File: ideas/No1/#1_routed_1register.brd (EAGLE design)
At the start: 85.1 x 137.5 mm, 20 parts, among them P1-O8RIGHT TD620831A, P1-P8LEFT TD620831A, U1 SN74HC595N, U2 SN74HC595N, U3 SN74HC595N

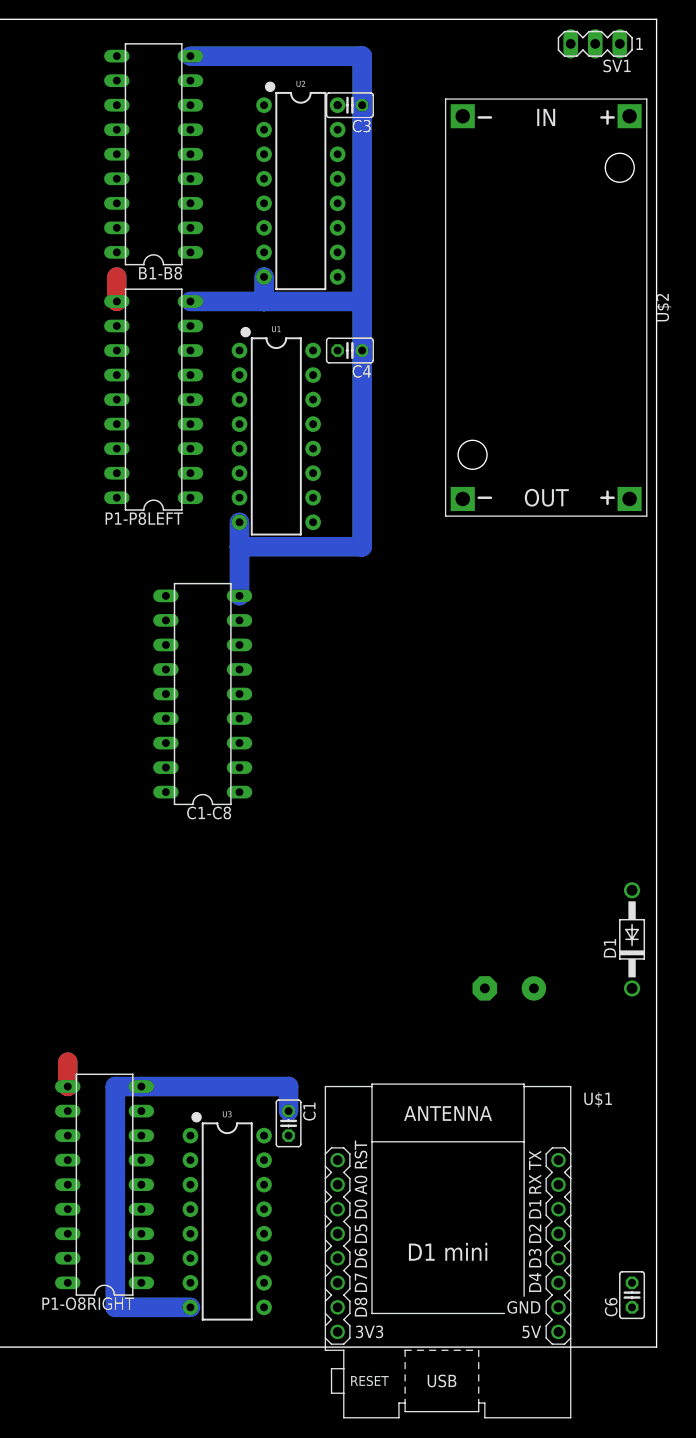
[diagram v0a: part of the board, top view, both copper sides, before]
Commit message: update picture with cable pins
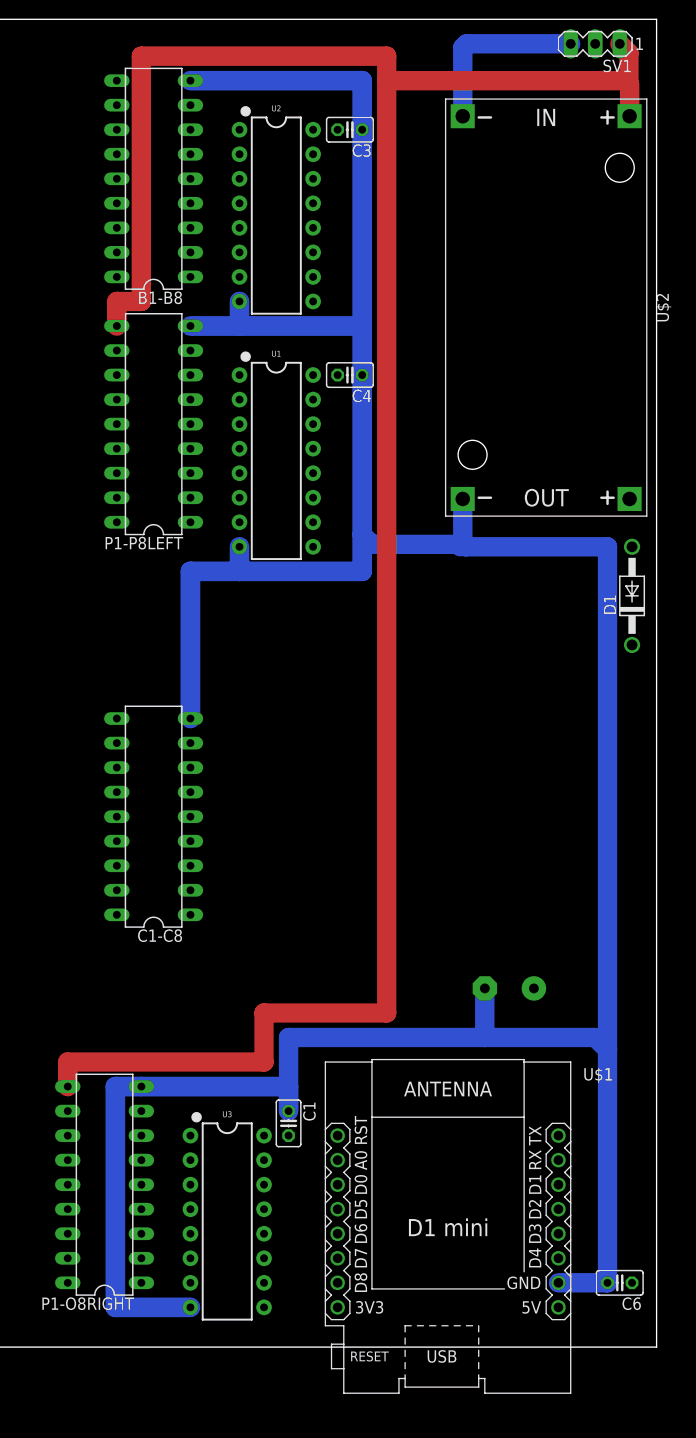
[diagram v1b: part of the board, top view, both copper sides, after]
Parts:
- moved D1 35.6 mm to (133.3, 59.7)
- moved C1-C8 13.7 mm to (83.8, 36.8)
- moved U2 3.59 mm to (96.5, 99.1)
- moved C4 2.54 mm to (104.1, 82.5)
- moved P1-P8LEFT 2.54 mm to (83.8, 77.5)
- moved U1 2.54 mm to (96.5, 73.7)
- moved U$1 2.54 mm to (114.3, -5.71)
- moved B1-B8 2.54 mm to (83.8, 102.9)
- moved C3 2.54 mm to (104.1, 108.0)
- moved C6 1.80 mm to (132.1, -11.4), turned to 180 degrees
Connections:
- removed net 3.3V: SV1.3, U$2.IN-, U$2.OUT-
- new net N$61: SV1.3, U$2.IN-
- net GND: now also U$2.OUT-
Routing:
- net 24V: track 5.08 -> 228.1 mm
- net VCC: track 5.08 -> 180.9 mm
- net GND: track 160.3 -> 331.5 mm
- net N$37: track 0.00 -> 139.7 mm
- net N$80: track 0.00 -> 71.1 mm
- net N$61: track 0.00 -> 18.4 mm
- net N$69: track 0.00 -> 5.06 mm
- net N$8: track 20.3 -> 17.8 mm
- net N$7: track 7.62 -> 5.08 mm
- net N$6: track 7.62 -> 5.08 mm
- net N$5: track 7.62 -> 5.08 mm
- net N$4: track 7.62 -> 5.08 mm
- net N$3: track 7.62 -> 5.08 mm
- net N$2: track 7.62 -> 5.08 mm
- net N$1: track 7.62 -> 5.08 mm

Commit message: 1_route_1register.sch updated
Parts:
- removed SV2, SV3, SV5: (no value), con-lsta:FE08
- added HEADB1-B8, HEADC1-C8, HEADP1-8LEFT: (no value), con-lsta:FE08
- moved U2 40.7 mm to (94.0, 58.4)
- moved B1-B8 28.4 mm to (78.7, 74.9)
- moved P1-P8LEFT 25.9 mm to (78.7, 102.9)
- moved U1 25.9 mm to (91.4, 99.1)
- moved C1 21.6 mm to (96.5, 26.7), turned to 180 degrees
- moved C6 21.6 mm to (130.8, 10.2), turned to 90 degrees
- moved C2 20.9 mm to (115.6, 39.4), turned to 90 degrees
- moved P1-O8RIGHT 20.3 mm to (78.7, 19.1)
- moved U$1 20.3 mm to (114.3, 14.6)
- moved U3 20.3 mm to (91.4, 15.2)
- moved D1 19.3 mm to (125.7, 41.9)
- moved C4 15.2 mm to (104.1, 67.3)
- moved SV1 14.0 mm to (115.6, 115.6)
- moved C1-C8 9.16 mm to (78.7, 44.5)
- moved U$2 7.73 mm to (116.8, 90.8)
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- renumbered SV4 to HEADP1-P8RIGHT
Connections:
- removed net N$60: C1-C8.11, HEADP1-P8RIGHT.2
- new net N$20: HEADP1-8LEFT.1, P1-P8LEFT.18
- net N$10: now also HEADP1-8LEFT.3, P1-P8LEFT.16; no longer P1-P8LEFT.12, SV2.3
- net N$11: now also HEADP1-8LEFT.4, P1-P8LEFT.15; no longer P1-P8LEFT.13, SV2.5
- net N$12: now also HEADP1-8LEFT.5, P1-P8LEFT.14; no longer B1-B8.15, SV3.2
- net N$13: now also HEADP1-8LEFT.6, P1-P8LEFT.13; no longer P1-P8LEFT.14, SV2.7
- net N$14: now also HEADP1-8LEFT.7, P1-P8LEFT.12; no longer P1-P8LEFT.15, SV3.1
- net N$15: now also HEADP1-8LEFT.8, P1-P8LEFT.11; no longer P1-P8LEFT.16, SV3.3
- net N$16: now also B1-B8.18, HEADB1-B8.1; no longer P1-P8LEFT.17, SV3.5
- net N$17: now also B1-B8.17, HEADB1-B8.2; no longer P1-P8LEFT.18, SV3.7
- net N$18: now also B1-B8.16, HEADB1-B8.3; no longer B1-B8.11, SV2.2
- net N$19: now also B1-B8.15, HEADB1-B8.4; no longer B1-B8.12, SV2.4
- net N$21: now also B1-B8.14, HEADB1-B8.5; no longer B1-B8.13, SV2.6
- net N$22: now also B1-B8.13, HEADB1-B8.6; no longer B1-B8.14, SV2.8
- net N$23: now also B1-B8.12, HEADB1-B8.7; no longer B1-B8.16, SV3.4
- net N$24: now also B1-B8.11, HEADB1-B8.8; no longer B1-B8.17, SV3.6
- net N$26: now also HEADP1-P8RIGHT.1, P1-O8RIGHT.18; no longer B1-B8.18, SV3.8
- net N$28: now also P1-O8RIGHT.16; no longer P1-O8RIGHT.12
- net N$30: now also HEADP1-P8RIGHT.2, P1-O8RIGHT.17; no longer HEADP1-P8RIGHT.1, P1-O8RIGHT.11
- net N$33: now also HEADP1-P8RIGHT.5, P1-O8RIGHT.14; no longer C1-C8.17, SV5.6
- net N$35: now also HEADP1-P8RIGHT.6, P1-O8RIGHT.13; no longer HEADP1-P8RIGHT.7, P1-O8RIGHT.14
- net N$39: now also HEADP1-P8RIGHT.4; no longer SV5.1
- net N$40: now also HEADP1-P8RIGHT.7, P1-O8RIGHT.12; no longer P1-O8RIGHT.16, SV5.3
- net N$49: now also HEADP1-P8RIGHT.8, P1-O8RIGHT.11; no longer HEADP1-P8RIGHT.5, P1-O8RIGHT.13
- net N$50: now also C1-C8.18, HEADC1-C8.1; no longer P1-O8RIGHT.17, SV5.5
- net N$51: now also C1-C8.17, HEADC1-C8.2; no longer P1-O8RIGHT.18, SV5.7
- net N$52: now also C1-C8.16, HEADC1-C8.3; no longer C1-C8.18, SV5.8
- net N$53: now also C1-C8.15, HEADC1-C8.4; no longer C1-C8.16, SV5.4
- net N$54: now also C1-C8.14, HEADC1-C8.5; no longer C1-C8.15, SV5.2
- net N$57: now also C1-C8.13, HEADC1-C8.6; no longer C1-C8.14, HEADP1-P8RIGHT.8
- net N$58: now also C1-C8.12, HEADC1-C8.7; no longer C1-C8.13, HEADP1-P8RIGHT.6
- net N$59: now also C1-C8.11, HEADC1-C8.8; no longer C1-C8.12, HEADP1-P8RIGHT.4
- net N$9: now also HEADP1-8LEFT.2, P1-P8LEFT.17; no longer P1-P8LEFT.11, SV2.1
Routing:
- net N$37: track 139.7 -> 0.00 mm
- net N$80: track 71.1 -> 0.00 mm
- net 24V: track 228.1 -> 162.3 mm
- net GND: track 331.5 -> 304.5 mm
- net N$7: track 5.08 -> 30.5 mm
- net N$2: track 5.08 -> 25.4 mm
- net N$69: track 5.06 -> 24.3 mm
- net N$9: track 0.00 -> 15.2 mm
- net N$8: track 17.8 -> 33.0 mm
- net N$6: track 5.08 -> 20.3 mm
- net N$39: track 0.00 -> 15.2 mm
- net N$26: track 0.00 -> 15.2 mm
- net N$24: track 0.00 -> 15.2 mm
- net N$23: track 0.00 -> 15.2 mm
- net N$22: track 0.00 -> 15.2 mm
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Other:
- board size 85.1 x 137.5 mm -> 85.1 x 117.1 mm

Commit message: 1_route_1register.sch updated
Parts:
- removed D1: 1N4004, diode:DO41-10
- added 1N4007: (no value), resistor:0207/15
- moved C2 9.16 mm to (108.0, 44.5), turned to 180 degrees
- moved HEADB1-B8 7.62 mm to (67.3, 73.7)
- moved HEADC1-C8 7.62 mm to (67.3, 43.2)
- moved HEADP1-8LEFT 7.62 mm to (67.3, 101.6)
- moved HEADP1-P8RIGHT 7.62 mm to (67.3, 17.8)
- moved C4 2.54 mm to (106.7, 67.3)
- moved U3 2.54 mm to (88.9, 15.2)
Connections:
- removed net N$79: U$1.JP1.3, U1.11, U3.11
- new net N$60: U$1.JP2.5, U1.11, U3.11
- net N$34: now also U$1.JP2.3; no longer U$1.JP1.5
- net N$36: now also U$1.JP2.4; no longer U$1.JP1.4
- net N$37: now also U$1.JP1.5; no longer U$1.JP2.5
- net N$38: now also U$1.JP1.3; no longer U$1.JP2.3
- net N$69: now also 1N4007.1; no longer D1.A
- net N$80: now also U$1.JP1.4; no longer U$1.JP2.4
- net VCC: now also 1N4007.2; no longer D1.C
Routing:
- net N$34: track 0.00 -> 109.2 mm, vias 0 -> 2
- net N$60: track 0.00 -> 106.7 mm, vias 0 -> 2
- net N$66: track 0.00 -> 68.6 mm, vias 0 -> 1
- net N$36: track 0.00 -> 38.1 mm, vias 0 -> 2
- net GND: track 304.5 -> 332.7 mm
- net N$9: track 15.2 -> 7.62 mm
- net N$59: track 15.2 -> 7.62 mm
- net N$58: track 15.2 -> 7.62 mm
- net N$57: track 15.2 -> 7.62 mm
- net N$54: track 15.2 -> 7.62 mm
- net N$53: track 15.2 -> 7.62 mm
- net N$52: track 15.2 -> 7.62 mm
- net N$51: track 15.2 -> 7.62 mm
- net N$50: track 15.2 -> 7.62 mm
- net N$49: track 15.2 -> 7.62 mm
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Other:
- board size 85.1 x 117.1 mm -> 74.9 x 117.1 mm

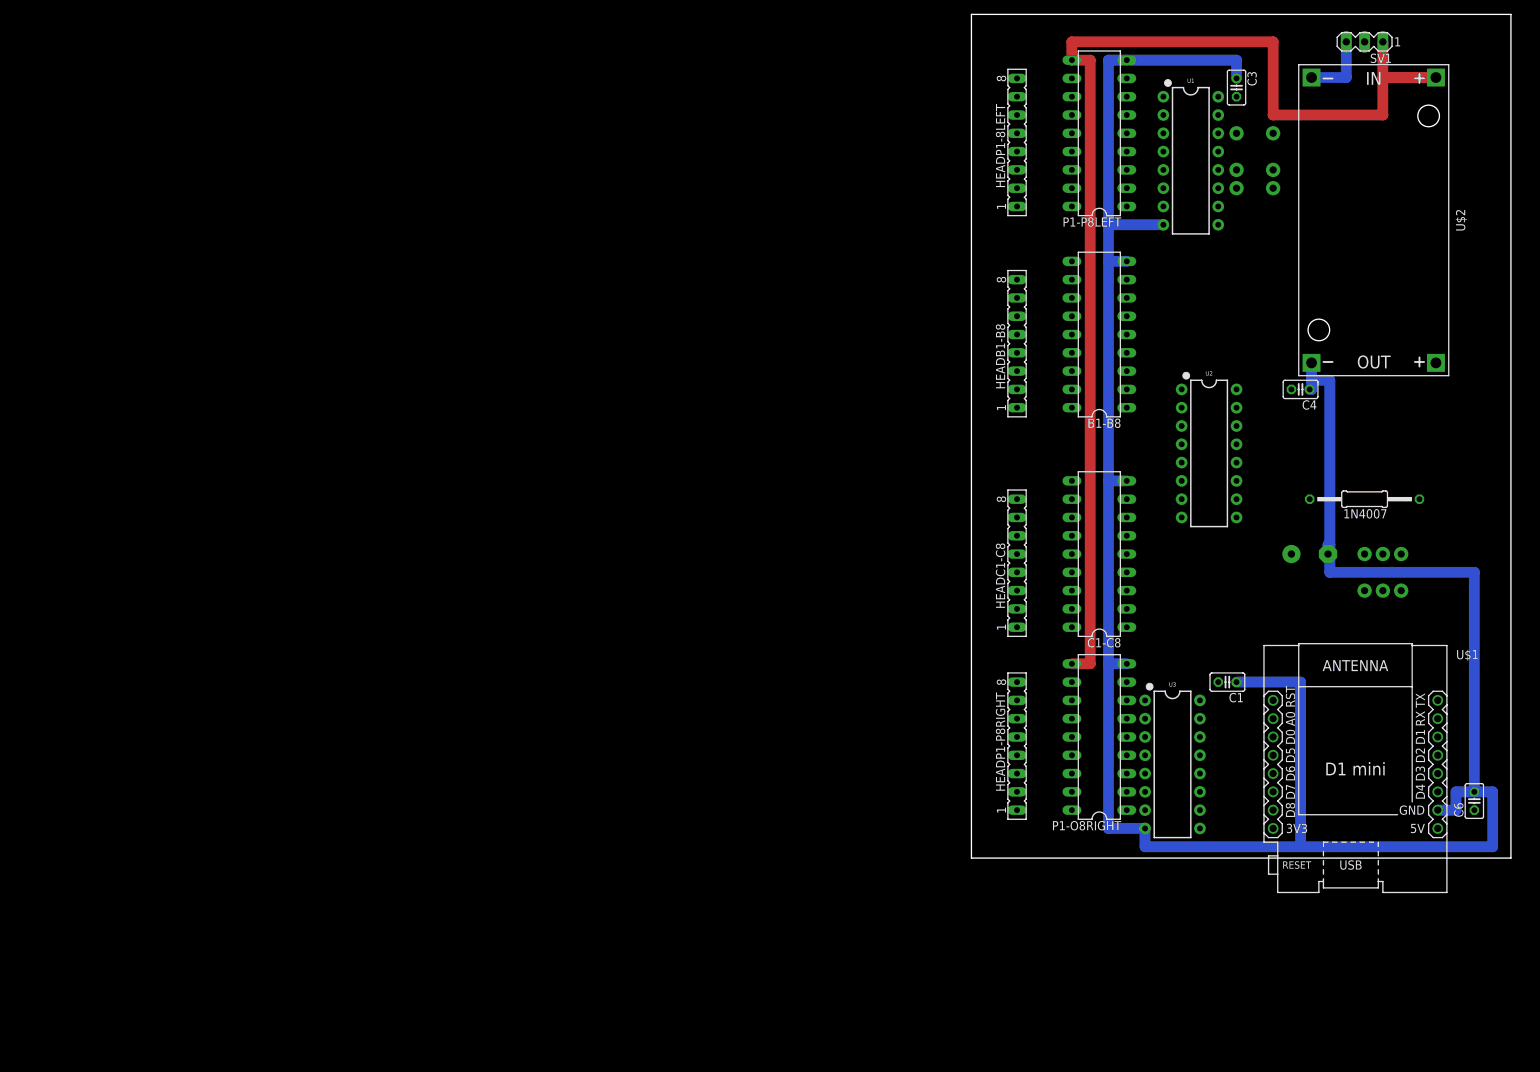
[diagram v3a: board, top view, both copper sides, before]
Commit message: 1_route_1register.sch changed
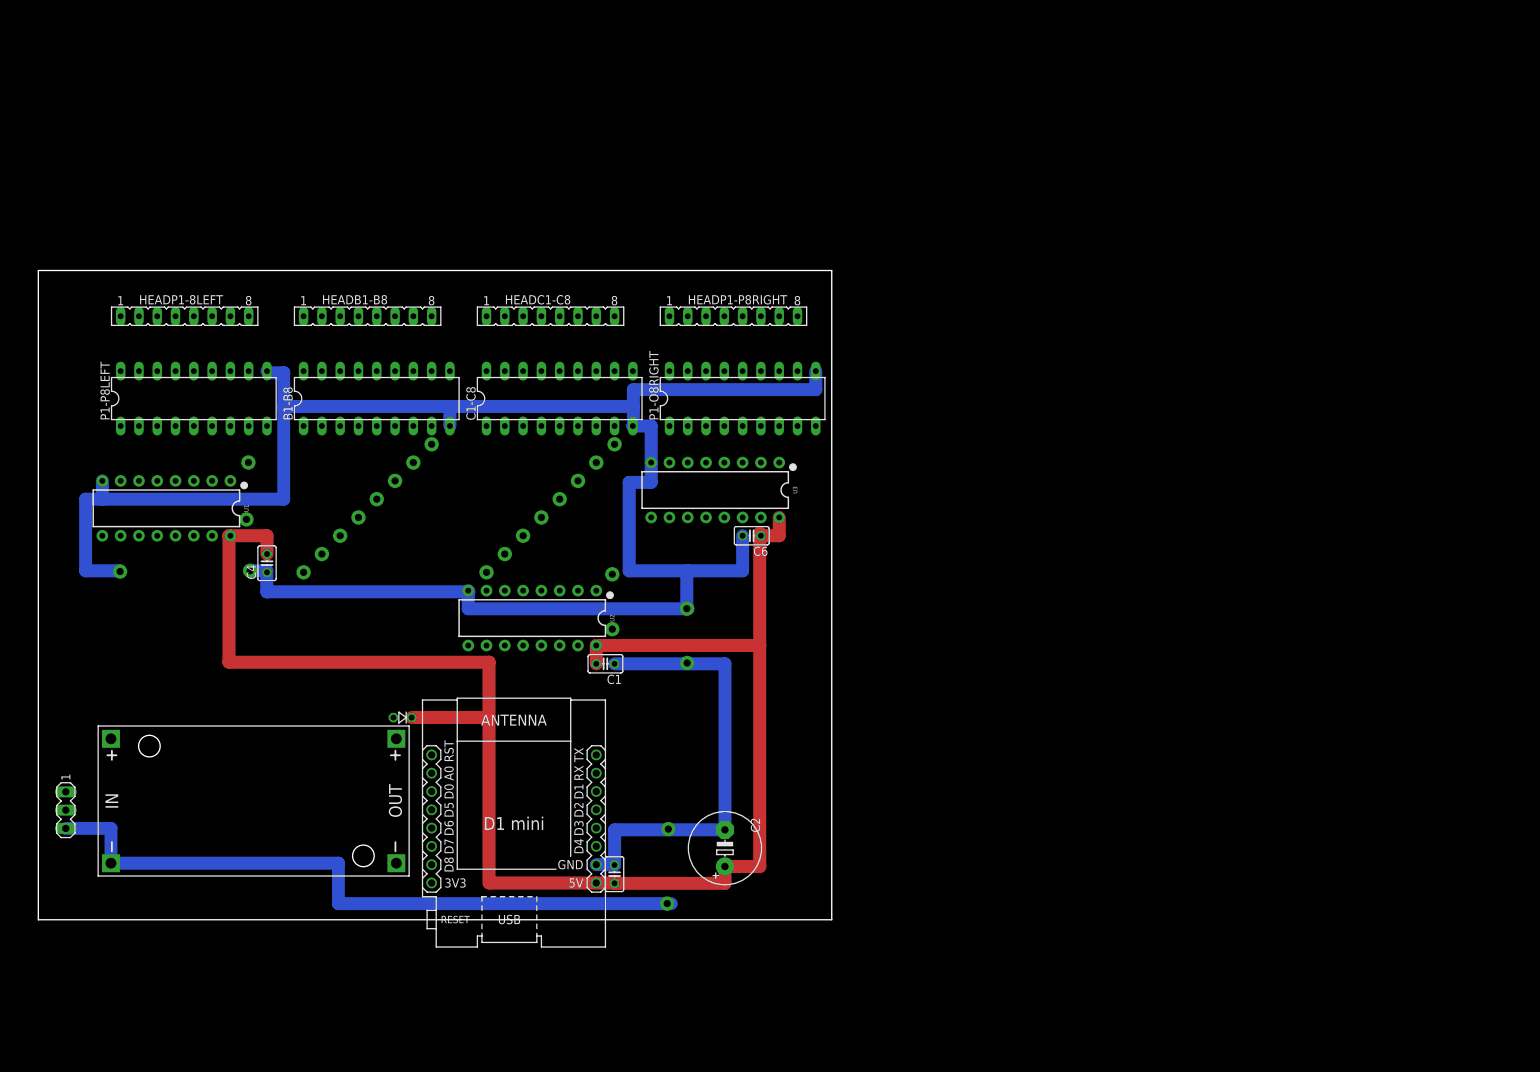
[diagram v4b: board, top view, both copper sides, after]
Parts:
- 1N4007: device resistor:0207/15 -> diode:D-2.5
- P1-O8RIGHT, P1-P8LEFT: value TD620831A -> TD627832A
- moved SV1 209.5 mm to (-64.8, 8.89), turned to 270 degrees
- moved U$2 175.2 mm to (-38.7, 10.2), turned to 0 degrees
- moved U1 150.2 mm to (-50.8, 50.8), turned to 180 degrees
- moved C4 145.5 mm to (-36.8, 43.2), turned to 90 degrees
- moved C3 139.2 mm to (11.4, 0.00)
- moved 1N4007 137.0 mm to (-18.0, 21.7)
- moved P1-P8LEFT 131.0 mm to (-47.0, 66.0), turned to 0 degrees
- moved HEADP1-8LEFT 118.1 mm to (-48.3, 77.5), turned to 0 degrees
- moved U$1 117.1 mm to (-2.54, 7.04)
- moved C6 106.9 mm to (30.5, 47.0), turned to 180 degrees
- moved B1-B8 100.7 mm to (-21.6, 66.0), turned to 0 degrees
- moved U2 96.7 mm to (0.00, 35.6), turned to 180 degrees
- moved C2 90.9 mm to (26.8, 3.61), flipped to the top, turned to 90 degrees
- moved HEADB1-B8 90.3 mm to (-22.9, 77.5), turned to 0 degrees
- moved C1 86.4 mm to (10.2, 29.2)
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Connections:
- removed net N$36: U$1.JP2.4, U1.12, U3.12
- removed net N$38: U$1.JP1.3, U2.12
- new net N$74: U$1.JP1.4, U1.12, U3.12
- new net N$76: U$1.JP1.5, U1.11, U3.11
- net 24V: now also P1-O8RIGHT.9, P1-P8LEFT.9; no longer P1-O8RIGHT.10, P1-P8LEFT.10
- net GND: now also P1-O8RIGHT.10, P1-P8LEFT.10; no longer P1-O8RIGHT.9, P1-P8LEFT.9
- net N$34: now also U$1.JP1.3; no longer U$1.JP2.3
- net N$37: now also U$1.JP2.3; no longer U$1.JP1.5
- net N$60: now also U$1.JP2.4, U2.12; no longer U$1.JP2.5, U1.11, U3.11
- net N$69: now also 1N4007.A; no longer 1N4007.1
- net N$80: now also U$1.JP2.5; no longer U$1.JP1.4
- net VCC: now also 1N4007.C; no longer 1N4007.2
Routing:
- net N$63: track 5.08 -> 122.6 mm, vias 1 -> 6
- net N$61: track 9.78 -> 94.5 mm
- net N$76: track 0.00 -> 81.3 mm
- net N$74: track 0.00 -> 76.2 mm
- net N$60: track 106.7 -> 33.0 mm, vias 2 -> 0
- net N$66: track 68.6 -> 0.00 mm
- net 24V: track 162.3 -> 97.0 mm
- net N$64: track 0.00 -> 50.8 mm, vias 1 -> 3
- net VCC: track 170.2 -> 219.5 mm
- net N$36: track 38.1 -> 83.2 mm, vias 2 -> 9
- net GND: track 332.7 -> 289.5 mm
- net N$34: track 109.2 -> 68.5 mm, vias 2 -> 0
- net N$3: track 0.00 -> 38.1 mm
- net N$80: track 0.00 -> 38.1 mm
- net N$4: track 0.00 -> 35.6 mm
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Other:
- board size 74.9 x 117.1 mm -> 110.2 x 90.1 mm
